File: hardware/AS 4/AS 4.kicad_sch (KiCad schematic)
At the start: 131 parts, among them J1 USB_C_Receptacle_USB2.0_16P, J2 Conn_02x03_Odd_Even, J3 TC2030-NL, Q1 IAUC120N06S5L011, Q2 S8050, Q3 S8050, U1 LM74610QDGKTQ1, U10 BME280, U2 LMR604205SRAKRQ1, U3 TPS2121RUXR, U4 TPS62901Q1, U5 TPS73501DRBR, U6 USBLC6-2SC6, U7 USBLC6-2SC6, U8 CH340C, U9 ESP32-S3-WROOM-1

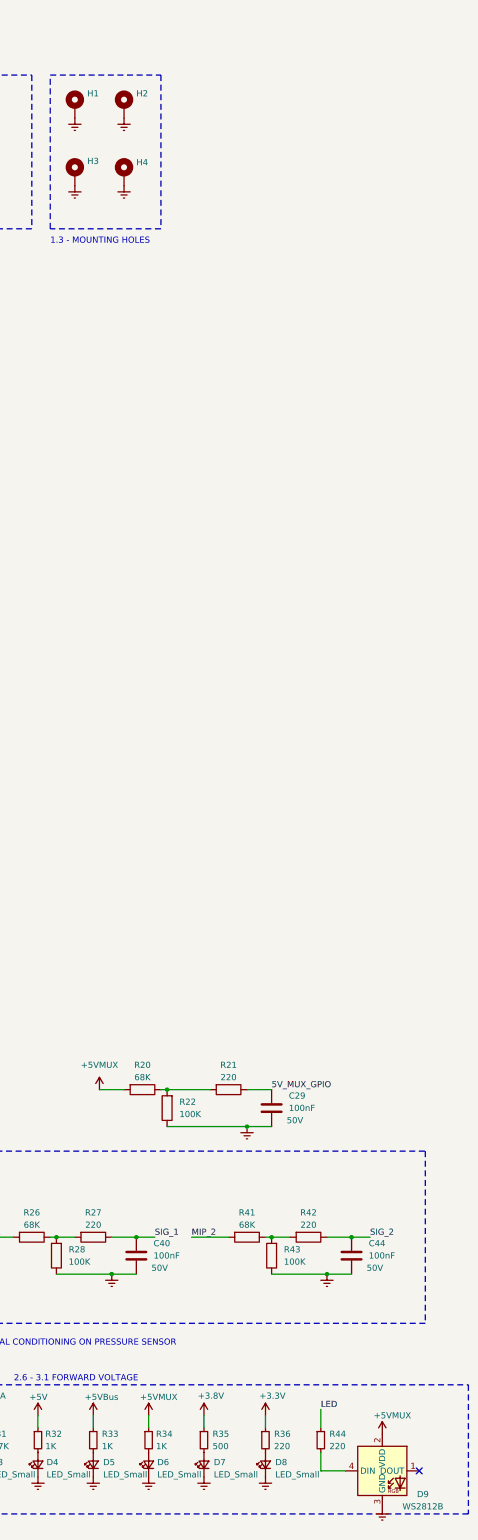
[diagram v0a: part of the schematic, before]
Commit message: V0.0.9 add OTA and looks stable
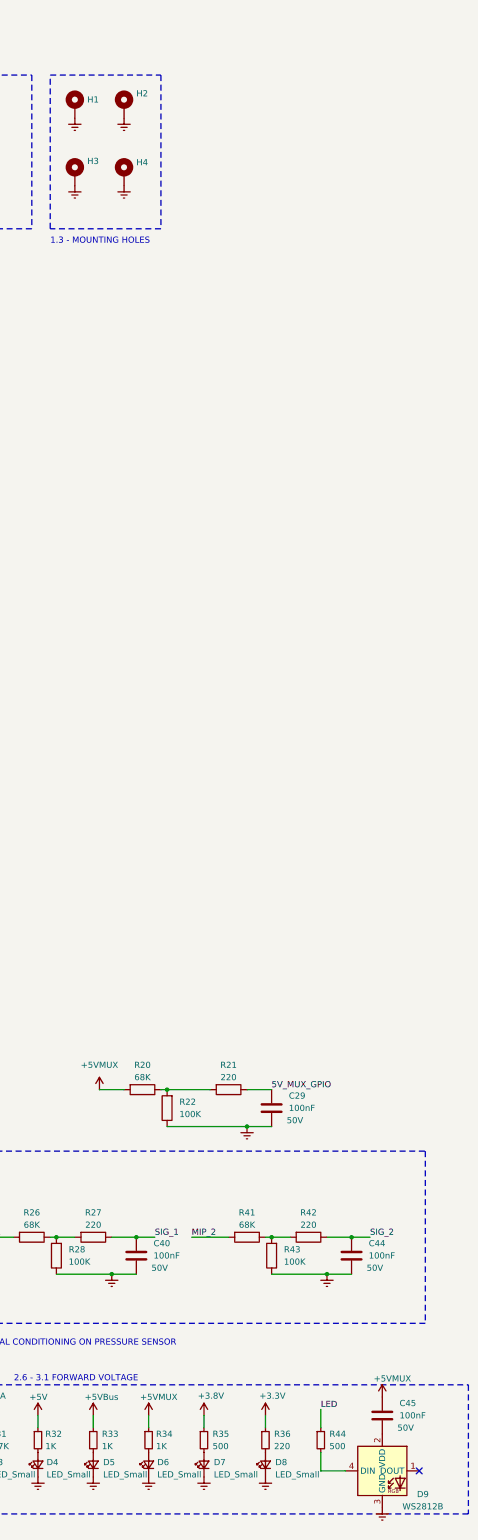
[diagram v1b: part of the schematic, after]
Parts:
- added C45: 100nF, Capacitor_SMD:C_0603_1608Metric, symbol Device:C
- H1, H2, H3, H4: footprint MountingHole:MountingHole_3.2mm_M3_Pad_Via -> MountingHole:MountingHole_5.3mm_M5_Pad_Via
- R44: value 220 -> 500
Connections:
- net +5VMUX: now also C45.1; no longer D9.2 (VDD)
- new net: C45.2, D9.2 (VDD)
